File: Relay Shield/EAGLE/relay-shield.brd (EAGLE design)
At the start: 88.9 x 83.8 mm, 46 parts, among them J1 POWER_JACKSLT, Q1 MPSA42, Q2 MPSA42, Q3 MPSA42, Q4 MPSA42, U1 RELAYPANASONIC-JS, U2 RELAYPANASONIC-JS, U3 RELAYPANASONIC-JS, U4 RELAYPANASONIC-JS

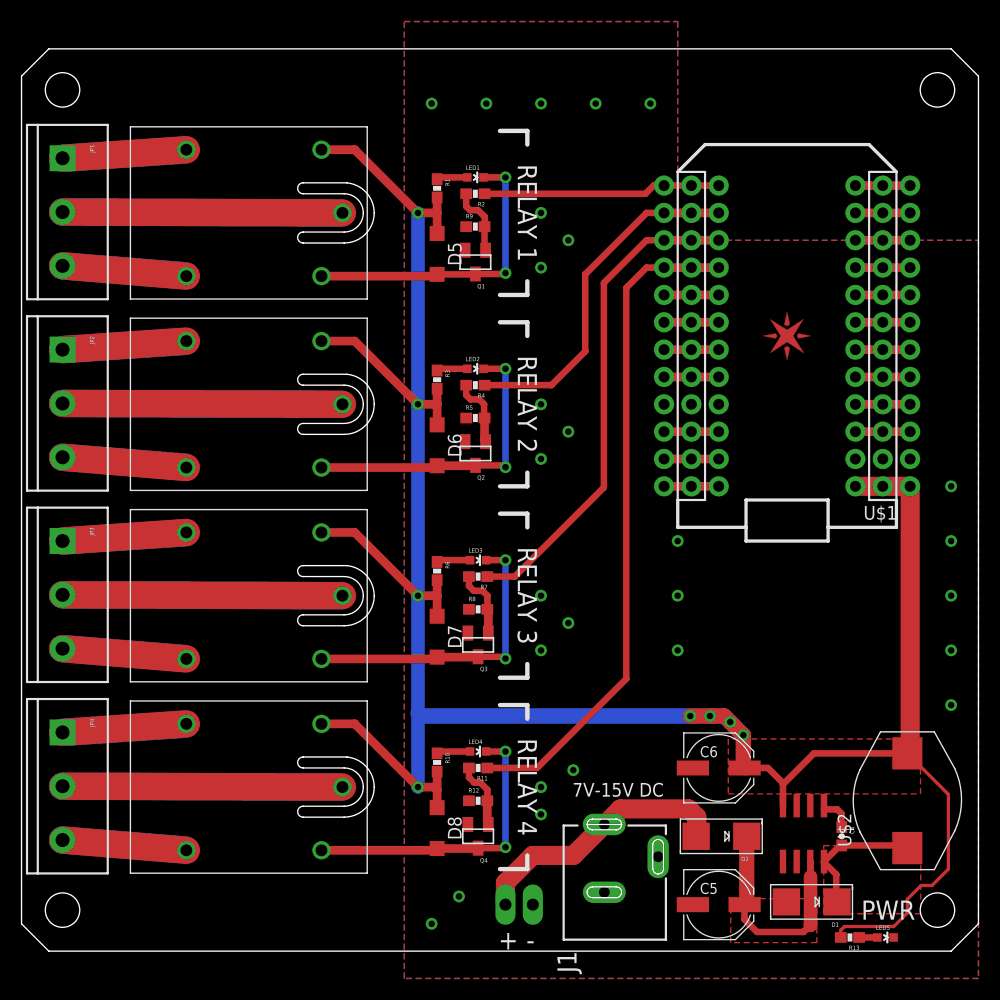
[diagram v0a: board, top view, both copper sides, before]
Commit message: changed the voltage regulator on the relay shield
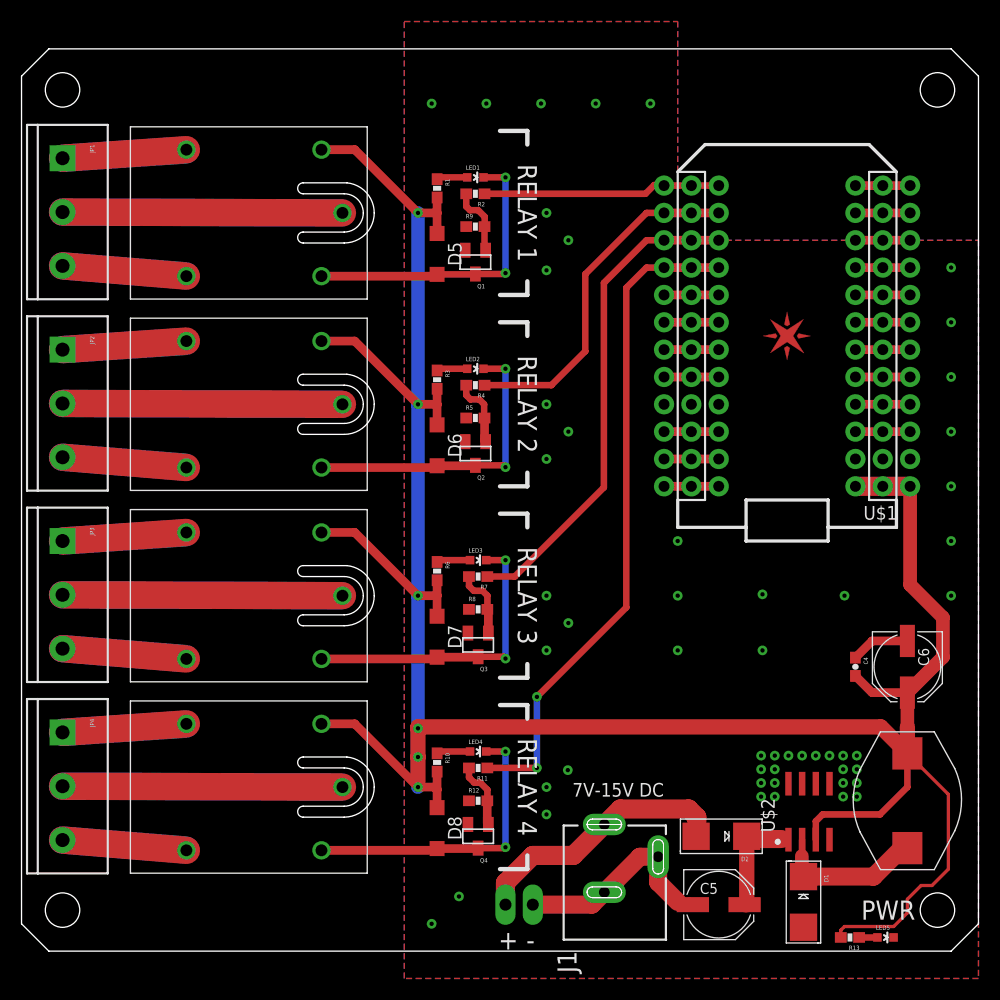
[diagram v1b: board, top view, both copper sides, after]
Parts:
- U$2: value LM2672 -> AP1509-50SG-13
- moved C6 19.9 mm to (82.3, 26.4), turned to 270 degrees
- moved C4 15.8 mm to (77.5, 26.4)
- moved U$2 2.09 mm to (73.2, 13.0), turned to 0 degrees
- moved D1 0.76 mm to (72.6, 4.57), turned to 270 degrees
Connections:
- removed net N$33: C4.1, U$2.1
- net +5V: now also C4.2, U$2.3; no longer U$2.4
- net GND: now also C4.1, U$2.4, U$2.5, U$2.7, U$2.8
- net N$14: now also U$2.1; no longer U$2.7
- net N$34: now also U$2.2; no longer C4.2, U$2.8
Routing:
- net GND: track 0.00 -> 25.4 mm, vias 27 -> 52
- net +5V: track 234.5 -> 257.1 mm, vias 8 -> 6
- net N$14: track 20.6 -> 10.6 mm
- net N$34: track 12.7 -> 16.5 mm
- net N$33: track 3.41 -> 0.00 mm
- net RELAY4: vias 0 -> 2
- removed copper zone on layer 1, net +5V
- removed copper zone on layer 1, net N$14
- removed copper zone on layer 1, net N$34

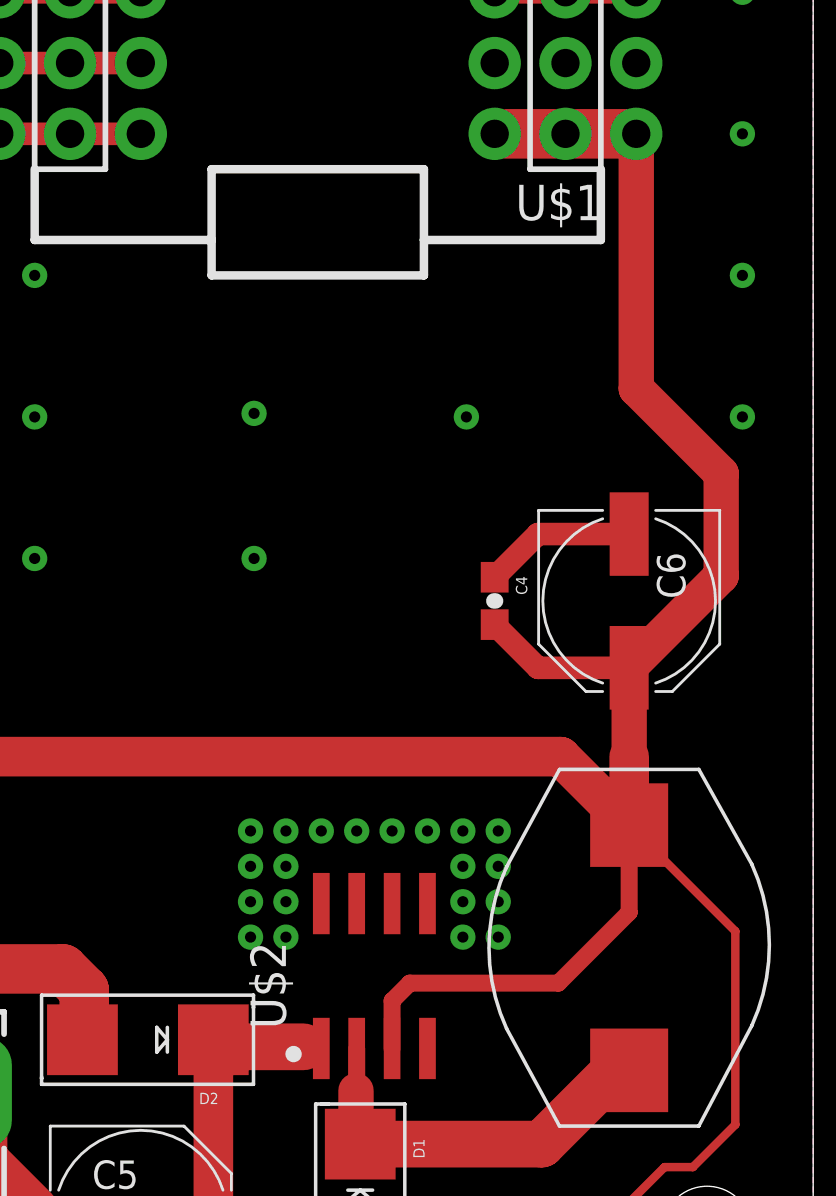
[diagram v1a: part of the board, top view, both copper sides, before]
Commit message: updated part designators as per to Sir William's request
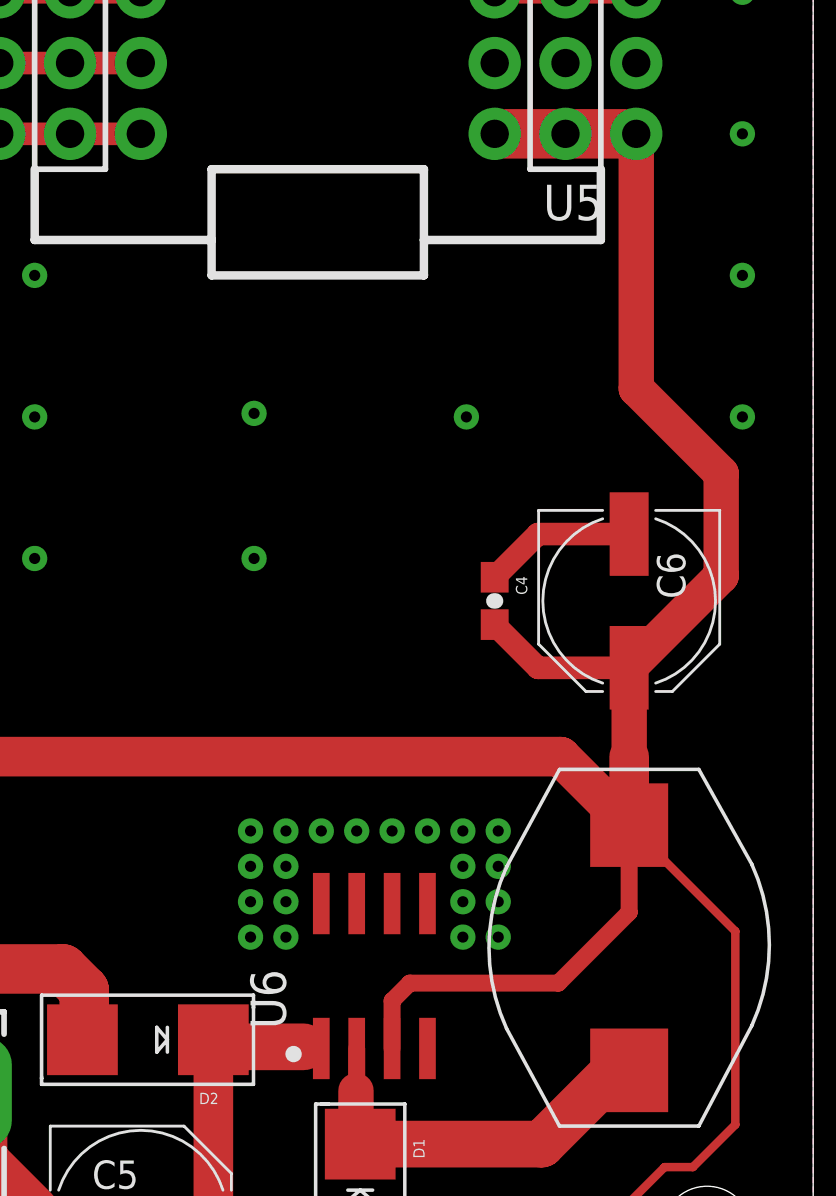
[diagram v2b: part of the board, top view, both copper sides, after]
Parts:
- renumbered U$1 to U5, U$2 to U6

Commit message: added license info to all design files
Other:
- board text added: "Reference Designs ARE PROVIDED "AS IS" AND "WITH ALL FAULTS. SPARK LABS, INC ("SPARK") DISCLAIMS ALL OTHER WARRANTIES, EXPRESS OR IMPLIED, REGARDING PRODUCTS OR THE REFERENCE DESIGNS, INCLUDING BUT NOT LIMITED TO, ANY IMPLIED WARRANTIES OF MERCHANTABILITY, FITNESS FOR A PARTICULAR PURPOSE, OR NON-INFRINGEMENT. Spark may make changes to specifications and product descriptions at any time, without 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"
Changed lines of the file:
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@@
 <text x="44.2976" y="0.1524" size="1.778" layer="21">+</text>
 <text x="46.8884" y="0.1524" size="1.778" layer="21">-</text>
+<text x="127" y="12.7" size="2.54" layer="51">Reference Designs ARE PROVIDED "AS IS" AND "WITH ALL FAULTS. SPARK LABS, INC
+("SPARK") DISCLAIMS ALL OTHER WARRANTIES, EXPRESS OR IMPLIED, REGARDING
+PRODUCTS OR THE REFERENCE DESIGNS, INCLUDING BUT NOT LIMITED TO, ANY
+IMPLIED WARRANTIES OF MERCHANTABILITY, FITNESS FOR A PARTICULAR PURPOSE,
+OR NON-INFRINGEMENT.
+Spark may make changes to specifications and product descriptions at any
+time, without notice. The Customer must not rely on the absence or
+characteristics of any features or instructions marked "reserved" or
+"undefined." Spark reserves these for future definition and shall have
+no responsibility whatsoever for conflicts or incompatibilities arising
+from future changes to them. The product information on the Web Site or
+Materials is subject to change without notice. Do not finalize a design
+with this information.
+Spark is a registered trademark.</text>
+<wire x1="121.92" y1="-2.54" x2="121.92" y2="83.82" width="0.4064" layer="51"/>
+<wire x1="121.92" y1="83.82" x2="302.26" y2="83.82" width="0.4064" layer="51"/>
+<wire x1="302.26" y1="83.82" x2="302.26" y2="-2.54" width="0.4064" layer="51"/>
+<wire x1="302.26" y1="-2.54" x2="121.92" y2="-2.54" width="0.4064" layer="51"/>
 </plain>
 <attributes>

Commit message: updated relay shield gerbers to v201
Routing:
- net +5V: track 257.1 -> 257.8 mm
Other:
- board text added: "Relay Shield v2.0.1 spark.io"
- board text removed: "Relay Shield v2.0 sparkdevices.com"
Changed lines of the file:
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@@
 <?xml version="1.0" encoding="utf-8"?>
 <!DOCTYPE eagle SYSTEM "eagle.dtd">
-<eagle version="6.3">
+<eagle version="6.5.0">
 <drawing>
 <settings>
@@
 <setting verticaltext="up"/>
 </settings>
-<grid distance="0.1" unitdist="inch" unit="inch" style="lines" multiple="1" display="yes" altdistance="0.05" altunitdist="inch" altunit="inch"/>
+<grid distance="0.005" unitdist="inch" unit="inch" style="lines" multiple="1" display="yes" altdistance="0.05" altunitdist="inch" altunit="inch"/>
 <layers>
 <layer number="1" name="Top" color="4" fill="1" visible="yes" active="yes"/>
@@
 <layer number="21" name="tPlace" color="16" fill="1" visible="yes" active="yes"/>
 <layer number="22" name="bPlace" color="14" fill="1" visible="yes" active="yes"/>
-<layer number="23" name="tOrigins" color="15" fill="1" visible="yes" active="yes"/>
-<layer number="24" name="bOrigins" color="15" fill="1" visible="yes" active="yes"/>
+<layer number="23" name="tOrigins" color="15" fill="1" visible="no" active="yes"/>
+<layer number="24" name="bOrigins" color="15" fill="1" visible="no" active="yes"/>
 <layer number="25" name="tNames" color="7" fill="1" visible="no" active="yes"/>
 <layer number="26" name="bNames" color="7" fill="1" visible="no" active="yes"/>
@@
 <layer number="50" name="dxf" color="7" fill="1" visible="no" active="no"/>
 <layer number="51" name="tDocu" color="6" fill="1" visible="yes" active="yes"/>
-<layer number="52" name="bDocu" color="7" fill="1" visible="yes" active="yes"/>
+<layer number="52" name="bDocu" color="7" fill="1" visible="no" active="yes"/>
 <layer number="53" name="tGND_GNDA" color="7" fill="9" visible="no" active="no"/>
 <layer number="54" name="bGND_GNDA" color="1" fill="9" visible="no" active="no"/>
@@
 <plain>
 <wire x1="86.36" y1="83.82" x2="2.54" y2="83.82" width="0" layer="20"/>
-<text x="78.486" y="77.724" size="1.778" layer="22" font="vector" ratio="15" rot="MR0">Relay Shield v2.0
-sparkdevices.com</text>
+<text x="78.486" y="77.724" size="1.778" layer="22" font="vector" ratio="15" rot="MR0">Relay Shield v2.0.1
+spark.io</text>
 <hole x="3.81" y="80.01" drill="3.2"/>
 <hole x="85.09" y="80.01" drill="3.2"/>
@@
 <wire x1="86.36" y1="83.82" x2="88.9" y2="81.28" width="0" layer="20"/>
 <wire x1="86.36" y1="0" x2="88.9" y2="2.54" width="0" layer="20"/>
-<dimension x1="7.62" y1="83.82" x2="7.62" y2="0" x3="-5.08" y3="41.91" layer="51"/>
-<dimension x1="85.09" y1="80.01" x2="85.09" y2="3.81" x3="95.25" y3="41.91" layer="51"/>
-<dimension x1="3.81" y1="80.01" x2="85.09" y2="80.01" x3="44.45" y3="87.63" layer="51" dtype="diameter"/>
-<dimension x1="0" y1="0" x2="88.9" y2="0" x3="44.45" y3="-10.16" layer="51" dtype="horizontal"/>
+<dimension x1="7.62" y1="83.82" x2="7.62" y2="0" x3="-5.08" y3="41.91" textsize="3.5" layer="51"/>
+<dimension x1="85.09" y1="80.01" x2="85.09" y2="3.81" x3="95.25" y3="41.91" textsize="3.5" layer="51"/>
+<dimension x1="3.81" y1="80.01" x2="85.09" y2="80.01" x3="44.45" y3="87.63" textsize="3.5" layer="51" dtype="diameter"/>
+<dimension x1="0" y1="0" x2="88.9" y2="0" x3="44.45" y3="-10.16" textsize="3.5" layer="51" dtype="horizontal"/>
 <wire x1="26.162" y1="70.358" x2="29.972" y2="70.358" width="0" layer="20"/>
 <wire x1="29.972" y1="70.358" x2="31.75" y2="68.58" width="0" layer="20" curve="-90"/>
@@
 <contactref element="L1" pad="P$2"/>
 <contactref element="R13" pad="2"/>
-<wire x1="27.865" y1="74.455" x2="30.955" y2="74.455" width="0.8128" layer="1"/>
-<wire x1="27.865" y1="56.675" x2="30.955" y2="56.675" width="0.8128" layer="1"/>
-<wire x1="27.865" y1="38.895" x2="30.955" y2="38.895" width="0.8128" layer="1"/>
-<wire x1="27.865" y1="21.115" x2="30.955" y2="21.115" width="0.8128" layer="1"/>
+<wire x1="27.686" y1="74.5744" x2="30.955" y2="74.455" width="0.8128" layer="1"/>
+<wire x1="27.686" y1="56.7944" x2="30.955" y2="56.675" width="0.8128" layer="1"/>
+<wire x1="27.686" y1="39.0144" x2="30.955" y2="38.895" width="0.8128" layer="1"/>
+<wire x1="27.686" y1="21.2344" x2="30.955" y2="21.115" width="0.8128" layer="1"/>
 <wire x1="38.608" y1="52.236" x2="38.608" y2="50.8" width="0.8128" layer="1"/>
 <wire x1="38.608" y1="50.8" x2="38.608" y2="48.89" width="0.8128" layer="1"/>
@@
 <contactref element="U1" pad="CLOSED"/>
 <contactref element="JP1" pad="3"/>
-<wire x1="3.81" y1="63.66" x2="15.315" y2="62.705" width="2.54" layer="1"/>
+<wire x1="3.81" y1="63.66" x2="15.494" y2="62.5856" width="2.54" layer="1"/>
 <wire x1="3.81" y1="63.66" x2="15.24" y2="62.738" width="2.54" layer="16"/>
 </signal>
@@
 <contactref element="JP1" pad="2"/>
 <contactref element="U1" pad="COMMON"/>
-<wire x1="3.81" y1="68.66" x2="29.815" y2="68.58" width="2.54" layer="1"/>
+<wire x1="3.81" y1="68.66" x2="29.6926" y2="68.58" width="2.54" layer="1"/>
 <wire x1="3.81" y1="68.66" x2="29.718" y2="68.58" width="2.54" layer="16"/>
 </signal>
@@
 <contactref element="U1" pad="OPEN"/>
 <contactref element="JP1" pad="1"/>
-<wire x1="3.81" y1="73.66" x2="15.315" y2="74.455" width="2.54" layer="1"/>
+<wire x1="3.81" y1="73.66" x2="15.494" y2="74.5744" width="2.54" layer="1"/>
 <wire x1="3.81" y1="73.66" x2="15.24" y2="74.422" width="2.54" layer="16"/>
 </signal>
@@
 <wire x1="42.164" y1="62.908" x2="42.126" y2="62.87" width="0.6096" layer="1"/>
 <wire x1="42.126" y1="62.87" x2="38.608" y2="62.87" width="0.6096" layer="1"/>
-<wire x1="27.865" y1="62.705" x2="38.443" y2="62.705" width="0.8128" layer="1"/>
+<wire x1="27.686" y1="62.5856" x2="38.443" y2="62.705" width="0.8128" layer="1"/>
 <wire x1="38.443" y1="62.705" x2="38.608" y2="62.87" width="0.8128" layer="1"/>
 <wire x1="42.914" y1="71.882" x2="44.958" y2="71.882" width="0.6096" layer="1"/>
@@
 <contactref element="Q2" pad="3"/>
 <contactref element="D6" pad="A"/>
-<wire x1="27.865" y1="44.925" x2="38.443" y2="44.925" width="0.8128" layer="1"/>
+<wire x1="27.686" y1="44.8056" x2="38.443" y2="44.925" width="0.8128" layer="1"/>
 <wire x1="38.443" y1="44.925" x2="38.608" y2="45.09" width="0.8128" layer="1"/>
 <wire x1="38.608" y1="45.09" x2="42.126" y2="45.09" width="0.8128" layer="1"/>
@@
 <contactref element="U2" pad="CLOSED"/>
 <contactref element="JP2" pad="3"/>
-<wire x1="3.81" y1="45.88" x2="15.315" y2="44.925" width="2.54" layer="1"/>
+<wire x1="3.81" y1="45.88" x2="15.494" y2="44.8056" width="2.54" layer="1"/>
 <wire x1="3.81" y1="45.88" x2="15.24" y2="44.958" width="2.54" layer="16"/>
 </signal>
@@
 <contactref element="JP2" pad="2"/>
 <contactref element="U2" pad="COMMON"/>
-<wire x1="3.81" y1="50.88" x2="29.815" y2="50.8" width="2.54" layer="1"/>
+<wire x1="3.81" y1="50.88" x2="29.6926" y2="50.8" width="2.54" layer="1"/>
 <wire x1="3.81" y1="50.88" x2="29.718" y2="50.8" width="2.54" layer="16"/>
 </signal>
@@
 <contactref element="U2" pad="OPEN"/>
 <contactref element="JP2" pad="1"/>
-<wire x1="3.81" y1="55.88" x2="15.315" y2="56.675" width="2.54" layer="1"/>
+<wire x1="3.81" y1="55.88" x2="15.494" y2="56.7944" width="2.54" layer="1"/>
 <wire x1="3.81" y1="55.88" x2="15.24" y2="56.642" width="2.54" layer="16"/>
 </signal>
@@
 <contactref element="Q3" pad="3"/>
 <contactref element="D7" pad="A"/>
-<wire x1="27.865" y1="27.145" x2="38.443" y2="27.145" width="0.8128" layer="1"/>
+<wire x1="27.686" y1="27.0256" x2="38.443" y2="27.145" width="0.8128" layer="1"/>
 <wire x1="38.443" y1="27.145" x2="38.608" y2="27.31" width="0.8128" layer="1"/>
 <wire x1="38.608" y1="27.31" x2="42.38" y2="27.31" width="0.8128" layer="1"/>
@@
 <contactref element="U3" pad="CLOSED"/>
 <contactref element="JP3" pad="3"/>
-<wire x1="3.81" y1="28.1" x2="15.315" y2="27.145" width="2.54" layer="1"/>
+<wire x1="3.81" y1="28.1" x2="15.494" y2="27.0256" width="2.54" layer="1"/>
 <wire x1="3.81" y1="28.1" x2="15.24" y2="27.178" width="2.54" layer="16"/>
 </signal>
@@
 <contactref element="JP3" pad="2"/>
 <contactref element="U3" pad="COMMON"/>
-<wire x1="3.81" y1="33.1" x2="29.815" y2="33.02" width="2.54" layer="1"/>
+<wire x1="3.81" y1="33.1" x2="29.6926" y2="33.02" width="2.54" layer="1"/>
 <wire x1="3.81" y1="33.1" x2="29.718" y2="33.02" width="2.54" layer="16"/>
 </signal>
@@
 <contactref element="U3" pad="OPEN"/>
 <contactref element="JP3" pad="1"/>
-<wire x1="3.81" y1="38.1" x2="15.315" y2="38.895" width="2.54" layer="1"/>
+<wire x1="3.81" y1="38.1" x2="15.494" y2="39.0144" width="2.54" layer="1"/>
 <wire x1="3.81" y1="38.1" x2="15.24" y2="38.862" width="2.54" layer="16"/>
 </signal>
@@
 <contactref element="Q4" pad="3"/>
 <contactref element="D8" pad="A"/>
-<wire x1="27.865" y1="9.365" x2="38.443" y2="9.365" width="0.8128" layer="1"/>
+<wire x1="27.686" y1="9.2456" x2="38.443" y2="9.365" width="0.8128" layer="1"/>
 <wire x1="38.443" y1="9.365" x2="38.608" y2="9.53" width="0.8128" layer="1"/>
 <wire x1="38.608" y1="9.53" x2="42.38" y2="9.53" width="0.8128" layer="1"/>
@@
 <contactref element="U4" pad="CLOSED"/>
 <contactref element="JP4" pad="3"/>
-<wire x1="3.81" y1="10.32" x2="15.315" y2="9.365" width="2.54" layer="1"/>
+<wire x1="3.81" y1="10.32" x2="15.494" y2="9.2456" width="2.54" layer="1"/>
 <wire x1="3.81" y1="10.32" x2="15.24" y2="9.398" width="2.54" layer="16"/>
 </signal>
@@
 <contactref element="JP4" pad="2"/>
 <contactref element="U4" pad="COMMON"/>
-<wire x1="3.81" y1="15.32" x2="29.815" y2="15.24" width="2.54" layer="1"/>
+<wire x1="3.81" y1="15.32" x2="29.6926" y2="15.24" width="2.54" layer="1"/>
 <wire x1="3.81" y1="15.32" x2="29.718" y2="15.24" width="2.54" layer="16"/>
 </signal>
@@
 <contactref element="U4" pad="OPEN"/>
 <contactref element="JP4" pad="1"/>
-<wire x1="3.81" y1="20.32" x2="15.315" y2="21.115" width="2.54" layer="1"/>
+<wire x1="3.81" y1="20.32" x2="15.494" y2="21.2344" width="2.54" layer="1"/>
 <wire x1="3.81" y1="20.32" x2="15.24" y2="21.082" width="2.54" layer="16"/>
 </signal>
